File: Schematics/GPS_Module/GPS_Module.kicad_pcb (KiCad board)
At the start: 4 copper layers, 69.5 x 97.3 mm, 69 parts, among them J1 Stack Male Edge Connector, J2 SWD_01x04_Pin, J3 25SH-B-06-TR, J6 USB_B_Micro, Q1 AO3400A, SW1 SW_STM_RESET, SW2 SW_STM_BOOT_MODE, U1 STM32F103CBTx, U10 AMS1117-3.3, U3 W25Q128JVS, U4 LM66100DCKR, U5 LM66100DCKR, U6 LM66100DCKR, U7 ACS70331EOLC, U9 ISO1042BQDWVR, Y1 X322516MMB4SI

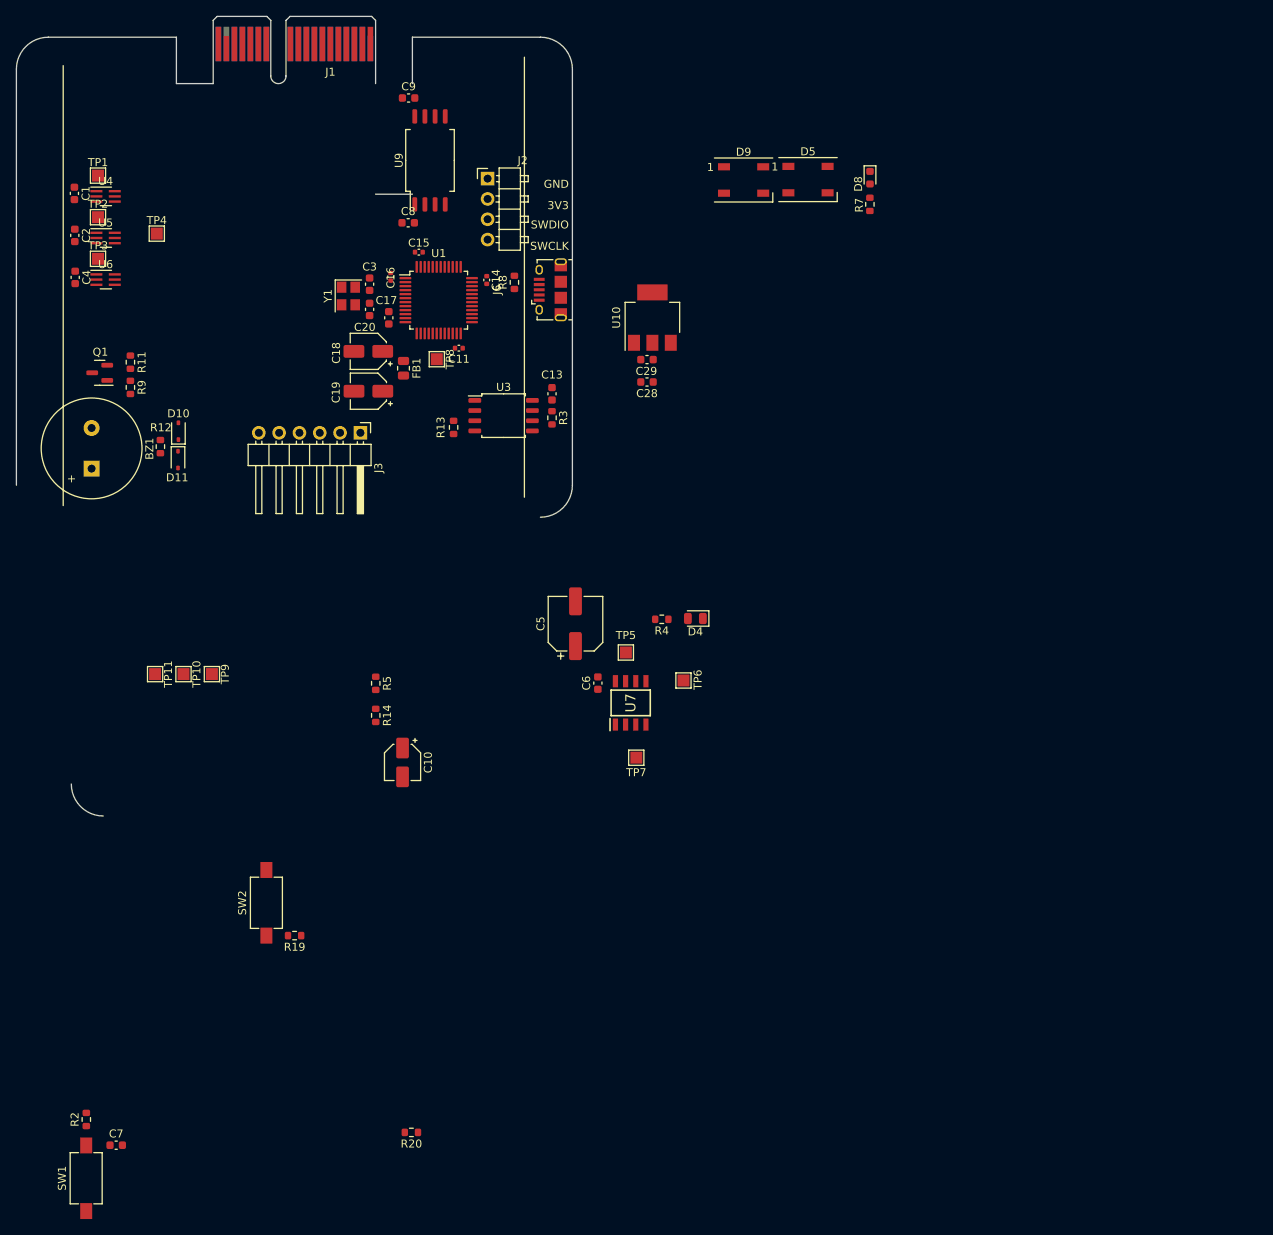
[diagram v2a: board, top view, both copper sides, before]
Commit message: Revert "starting PCB layout"
This reverts commit 0f9aa6cd92282e41b038e1a8acfc0611b64ad155.
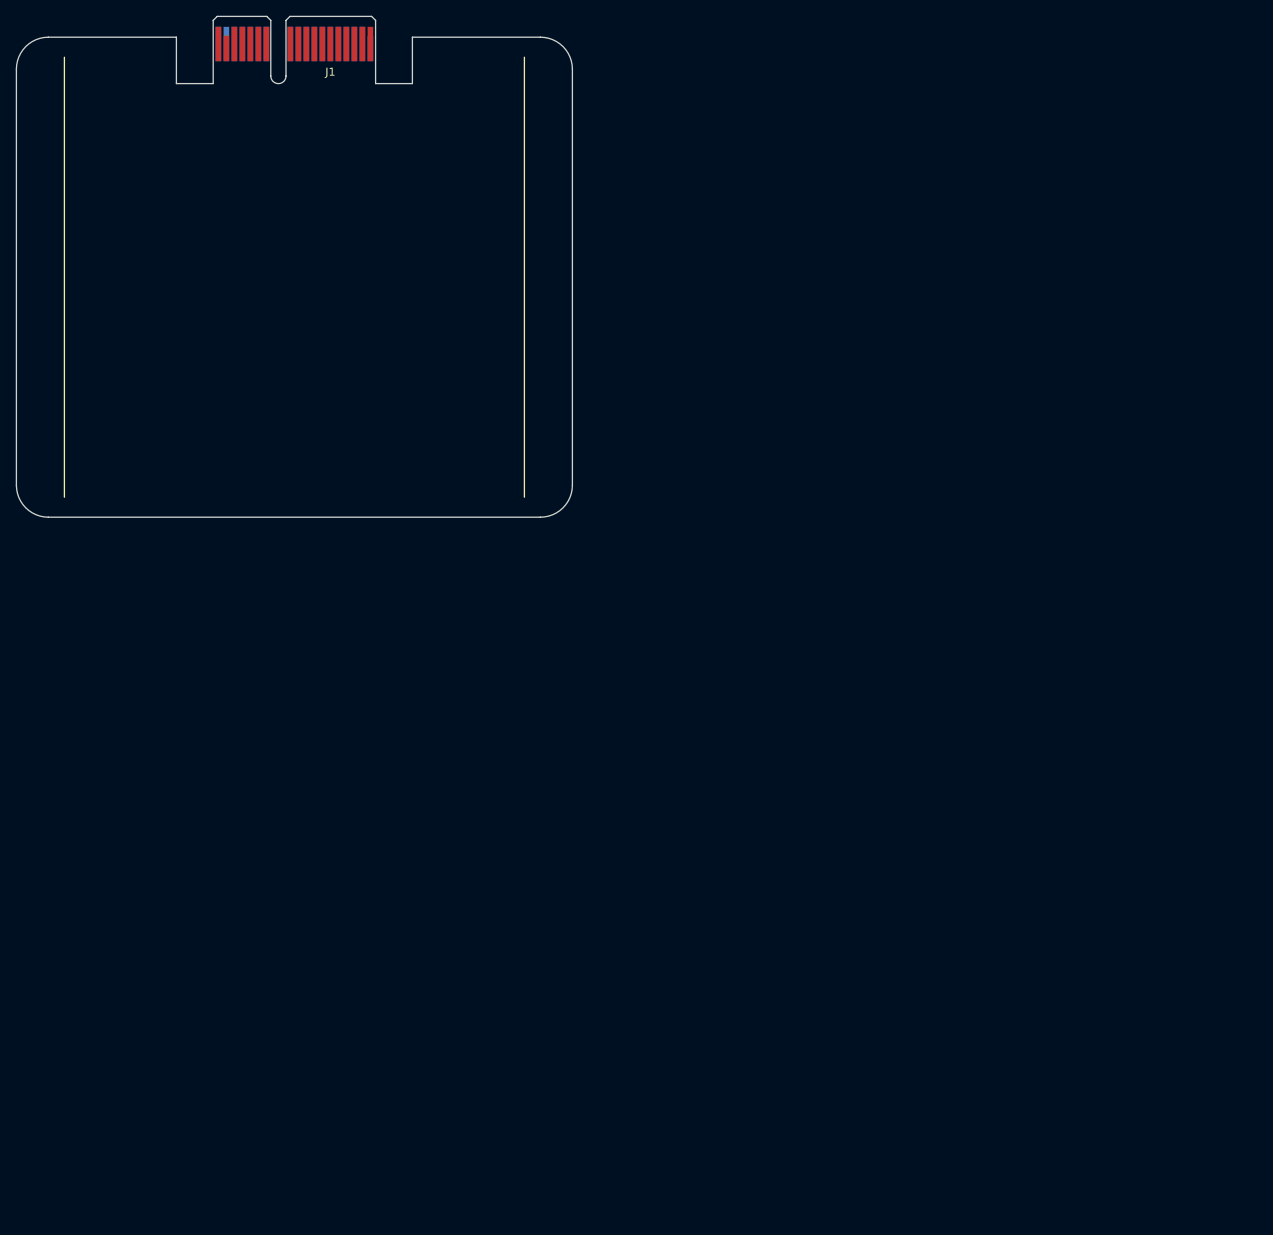
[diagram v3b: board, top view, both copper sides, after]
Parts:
- removed BZ1: PKM13EPYH4000, footprints:Buzzer_12.6x9.5RM5.0
- removed C1, C2, C4: 1uF, Capacitor_SMD:C_0603_1608Metric
- removed C10: 10u, Capacitor_SMD:CP_Elec_4x5.4
- removed C11, C14, C15, C16: 100n, Capacitor_SMD:C_0402_1005Metric
- removed C13, C7: 100nF, Capacitor_SMD:C_0603_1608Metric
- removed C17: 10n, Capacitor_SMD:C_0603_1608Metric
- removed C18, C19: 1uF, Capacitor_SMD:CP_Elec_4x5.4
- removed C20, C3: 10p, Capacitor_SMD:C_0603_1608Metric
- removed C28, C29: 10uF, Capacitor_SMD:C_0603_1608Metric
- removed C5: 100uF, Capacitor_SMD:CP_Elec_6.3x5.9
- removed C6: 0.1uF, Capacitor_SMD:C_0603_1608Metric
- removed C8, C9: 0.1u, Capacitor_SMD:C_0603_1608Metric
- removed D10, D11: 1N5819WS, Diode_SMD:D_SOD-323
- removed D4: PWR_LED (GRN), LED_SMD:LED_0805_2012Metric
- removed D5, D9: WS2812B, LED_SMD:LED_WS2812B_PLCC4_5.0x5.0mm_P3.2mm
- removed D8: DB_LED (YLW), LED_SMD:LED_0603_1608Metric
- removed FB1: 100R, Resistor_SMD:R_0805_2012Metric
- removed J2: SWD_01x04_Pin, SWD_Header:SWD_PinHeader_1x04_P2.54mm_Horizontal
- removed J3: 25SH-B-06-TR, Connector_PinHeader_2.54mm:PinHeader_1x06_P2.54mm_Horizontal
- removed J6: USB_B_Micro, Connector_USB:USB_Micro-B_Amphenol_10118194_Horizontal
- removed Q1: AO3400A, Package_TO_SOT_SMD:SOT-23
- removed R11, R13, R14, R2, R3: 10k, Resistor_SMD:R_0603_1608Metric
- removed R12: 1k, Resistor_SMD:R_0603_1608Metric
- removed R19, R20: 100k, Resistor_SMD:R_0603_1608Metric
- removed R4: 820R, Resistor_SMD:R_0603_1608Metric
- removed R5: 30k, Resistor_SMD:R_0603_1608Metric
- removed R7: 560R, Resistor_SMD:R_0603_1608Metric
- removed R8: 1.5k, Resistor_SMD:R_0603_1608Metric
- removed R9: 510R, Resistor_SMD:R_0603_1608Metric
- removed SW1: SW_STM_RESET, PTS636:PTS636_SK43_SMTR_LFS
- removed SW2: SW_STM_BOOT_MODE, PTS636:PTS636_SK43_SMTR_LFS
- removed TP1: TP_VSTACK, TestPoint:TestPoint_Pad_1.5x1.5mm
- removed TP10: TP_PA1, TestPoint:TestPoint_Pad_1.5x1.5mm
- removed TP11: TP_PA0, TestPoint:TestPoint_Pad_1.5x1.5mm
- removed TP2: TP_VUSB, TestPoint:TestPoint_Pad_1.5x1.5mm
- removed TP3: TP_VSWD, TestPoint:TestPoint_Pad_1.5x1.5mm
- removed TP4: TP_MUX, TestPoint:TestPoint_Pad_1.5x1.5mm
- removed TP5: TP_ISENSE, TestPoint:TestPoint_Pad_1.5x1.5mm
- removed TP6: TP_GND, TestPoint:TestPoint_Pad_1.5x1.5mm
- removed TP7: TP_3V3, TestPoint:TestPoint_Pad_1.5x1.5mm
- removed TP8: TP_BSENSE, TestPoint:TestPoint_Pad_1.5x1.5mm
- removed TP9: TP_PA2, TestPoint:TestPoint_Pad_1.5x1.5mm
- removed U1: STM32F103CBTx, Package_QFP:LQFP-48_7x7mm_P0.5mm
- removed U10: AMS1117-3.3, Package_TO_SOT_SMD:SOT-223-3_TabPin2
- removed U3: W25Q128JVS, Package_SO:SOIC-8_5.23x5.23mm_P1.27mm
- removed U4, U5, U6: LM66100DCKR, LMR66100:SC-70-6_Handsoldering
- removed U7: ACS70331EOLC, footprints:SOIC127P600X175-8N
- removed U9: ISO1042BQDWVR, ISO1042:SOIC-8 ISO1042BDWV
- removed Y1: X322516MMB4SI, Crystal:Crystal_SMD_3225-4Pin_3.2x2.5mm
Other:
- board size 69.5 x 97.3 mm -> 69.5 x 60 mm
- board text added: "GPS Daughterboard will be in a seperate project"

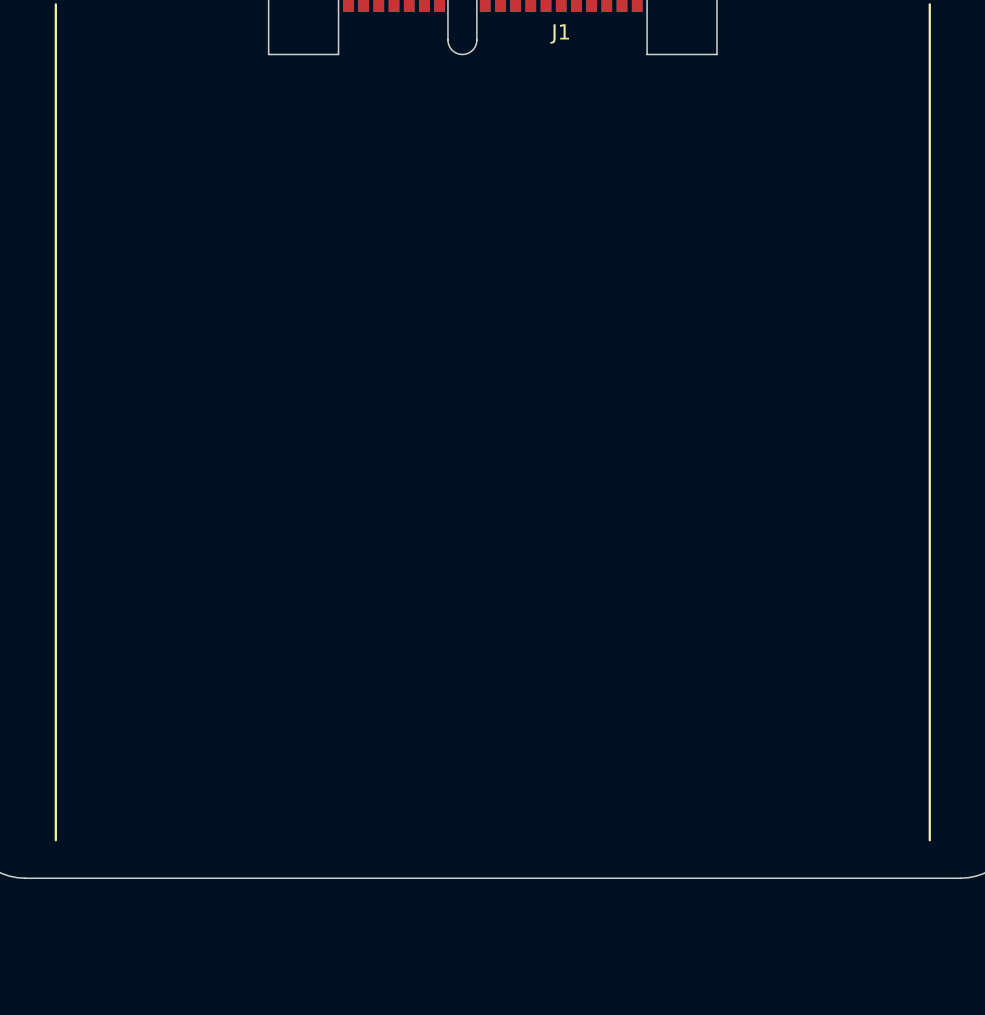
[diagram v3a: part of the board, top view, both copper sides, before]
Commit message: got everything on the board, starting wiring
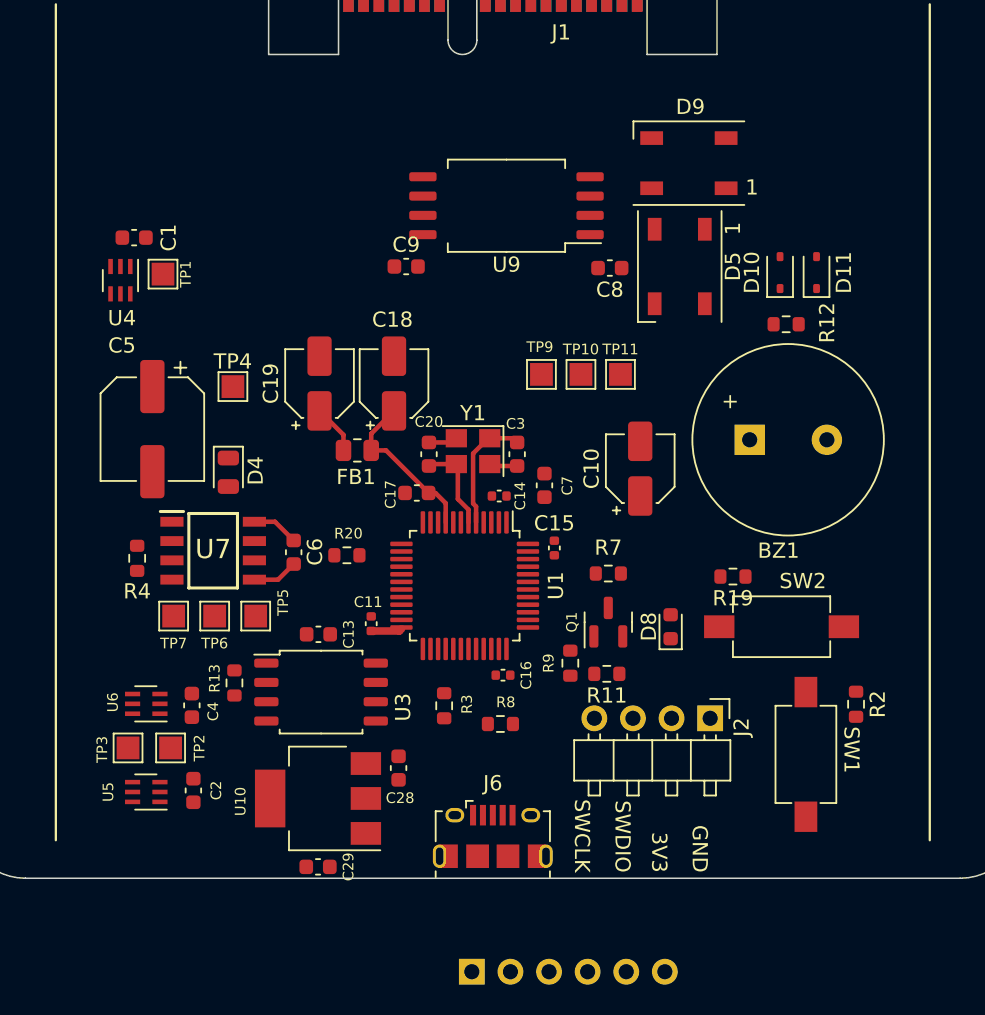
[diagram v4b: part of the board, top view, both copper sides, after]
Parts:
- added BZ1: PKM13EPYH4000, footprints:Buzzer_12.6x9.5RM5.0, F.Cu at (72.5, 51.3)
- added C1: 1uF, Capacitor_SMD:C_0603_1608Metric, F.Cu at (33.3, 38.0)
- added C10: 10u, Capacitor_SMD:CP_Elec_4x5.4, F.Cu at (66.6, 53.2)
- added C11: 100n, Capacitor_SMD:C_0402_1005Metric, F.Cu at (48.9, 63.4)
- added C13: 100nF, Capacitor_SMD:C_0603_1608Metric, F.Cu at (45.4, 64.1)
- added C14: 100n, Capacitor_SMD:C_0402_1005Metric, F.Cu at (57.3, 55.0)
- added C15: 100n, Capacitor_SMD:C_0402_1005Metric, F.Cu at (61.0, 58.4)
- added C16: 100n, Capacitor_SMD:C_0402_1005Metric, F.Cu at (57.6, 66.8)
- added C17: 10n, Capacitor_SMD:C_0603_1608Metric, F.Cu at (51.9, 54.8)
- added C18: 1uF, Capacitor_SMD:CP_Elec_4x5.4, F.Cu at (50.4, 47.6)
- added C19: 1uF, Capacitor_SMD:CP_Elec_4x5.4, F.Cu at (45.5, 47.6)
- added C2: 1uF, Capacitor_SMD:C_0603_1608Metric, F.Cu at (37.2, 74.4)
- added C20: 10p, Capacitor_SMD:C_0603_1608Metric, F.Cu at (52.7, 52.2)
- added C28: 10uF, Capacitor_SMD:C_0603_1608Metric, F.Cu at (50.7, 72.9)
- added C29: 10uF, Capacitor_SMD:C_0603_1608Metric, F.Cu at (45.4, 79.4)
- added C3: 10p, Capacitor_SMD:C_0603_1608Metric, F.Cu at (58.5, 52.2)
- added C4: 1uF, Capacitor_SMD:C_0603_1608Metric, F.Cu at (37.1, 68.8)
- added C5: 100uF, Capacitor_SMD:CP_Elec_6.3x5.9, F.Cu at (34.5, 50.6)
- added C6: 0.1uF, Capacitor_SMD:C_0603_1608Metric, F.Cu at (43.8, 58.7)
- added C7: 100nF, Capacitor_SMD:C_0603_1608Metric, F.Cu at (60.3, 54.3)
- added C8: 0.1u, Capacitor_SMD:C_0603_1608Metric, F.Cu at (64.6, 40.0)
- added C9: 0.1u, Capacitor_SMD:C_0603_1608Metric, F.Cu at (51.2, 39.9)
- added D10: 1N5819WS, Diode_SMD:D_SOD-323, F.Cu at (75.8, 40.3)
- added D11: 1N5819WS, Diode_SMD:D_SOD-323, F.Cu at (78.2, 40.3)
- added D4: PWR_LED (GRN), LED_SMD:LED_0805_2012Metric, F.Cu at (39.5, 53.4)
- added D5: WS2812B, LED_SMD:LED_WS2812B_PLCC4_5.0x5.0mm_P3.2mm, F.Cu at (69.2, 39.9)
- added D8: DB_LED (YLW), LED_SMD:LED_0603_1608Metric, F.Cu at (68.6, 63.6)
- added D9: WS2812B, LED_SMD:LED_WS2812B_PLCC4_5.0x5.0mm_P3.2mm, F.Cu at (69.8, 33.1)
- added FB1: 100R, Resistor_SMD:R_0805_2012Metric, F.Cu at (48.0, 52.0)
- added J2: SWD_01x04_Pin, SWD_Header:SWD_PinHeader_1x04_P2.54mm_Horizontal, F.Cu at (71.2, 69.6)
- added J3: 25SH-B-06-TR, Connector_PinHeader_2.54mm:PinHeader_1x06_P2.54mm_Horizontal, B.Cu at (55.5, 86.3)
- added J6: USB_B_Micro, Connector_USB:USB_Micro-B_Amphenol_10118194_Horizontal, F.Cu at (56.9, 77.4)
- added Q1: AO3400A, Package_TO_SOT_SMD:SOT-23, F.Cu at (64.5, 63.3)
- added R11: 10k, Resistor_SMD:R_0603_1608Metric, F.Cu at (64.4, 66.7)
- added R12: 1k, Resistor_SMD:R_0603_1608Metric, F.Cu at (76.2, 43.7)
- added R13: 10k, Resistor_SMD:R_0603_1608Metric, F.Cu at (39.9, 67.3)
- added R19: 100k, Resistor_SMD:R_0603_1608Metric, F.Cu at (72.7, 60.3)
- added R2: 10k, Resistor_SMD:R_0603_1608Metric, F.Cu at (80.8, 68.7)
- added R20: 100k, Resistor_SMD:R_0603_1608Metric, F.Cu at (47.3, 58.9)
- added R3: 10k, Resistor_SMD:R_0603_1608Metric, F.Cu at (53.7, 68.8)
- added R4: 820R, Resistor_SMD:R_0603_1608Metric, F.Cu at (33.5, 59.1)
- added R7: 560R, Resistor_SMD:R_0603_1608Metric, F.Cu at (64.5, 60.1)
- added R8: 1.5k, Resistor_SMD:R_0603_1608Metric, F.Cu at (57.4, 70.0)
- added R9: 510R, Resistor_SMD:R_0603_1608Metric, F.Cu at (62.0, 66.0)
- added SW1: SW_STM_RESET, PTS636:PTS636_SK43_SMTR_LFS, F.Cu at (77.5, 72.0)
- added SW2: SW_STM_BOOT_MODE, PTS636:PTS636_SK43_SMTR_LFS, F.Cu at (75.9, 63.6)
- added TP1: TP_VSTACK, TestPoint:TestPoint_Pad_1.5x1.5mm, F.Cu at (35.2, 40.4)
- added TP10: TP_PA1, TestPoint:TestPoint_Pad_1.5x1.5mm, F.Cu at (62.7, 47.0)
- added TP11: TP_PA0, TestPoint:TestPoint_Pad_1.5x1.5mm, F.Cu at (65.3, 47.0)
- added TP2: TP_VUSB, TestPoint:TestPoint_Pad_1.5x1.5mm, F.Cu at (35.7, 71.6)
- added TP3: TP_VSWD, TestPoint:TestPoint_Pad_1.5x1.5mm, F.Cu at (32.9, 71.6)
- added TP4: TP_MUX, TestPoint:TestPoint_Pad_1.5x1.5mm, F.Cu at (39.8, 47.8)
- added TP5: TP_ISENSE, TestPoint:TestPoint_Pad_1.5x1.5mm, F.Cu at (41.3, 62.9)
- added TP6: TP_GND, TestPoint:TestPoint_Pad_1.5x1.5mm, F.Cu at (38.6, 62.9)
- added TP7: TP_3V3, TestPoint:TestPoint_Pad_1.5x1.5mm, F.Cu at (35.9, 62.9)
- added TP9: TP_PA2, TestPoint:TestPoint_Pad_1.5x1.5mm, F.Cu at (60.1, 47.0)
- added U1: STM32F103CBTx, Package_QFP:LQFP-48_7x7mm_P0.5mm, F.Cu at (55.0, 60.9)
- added U10: AMS1117-3.3, Package_TO_SOT_SMD:SOT-223-3_TabPin2, F.Cu at (45.4, 74.9)
- added U3: W25Q128JVS, Package_SO:SOIC-8_5.23x5.23mm_P1.27mm, F.Cu at (45.6, 67.9)
- added U4: LM66100DCKR, LMR66100:SC-70-6, F.Cu at (32.4, 40.8)
- added U5: LM66100DCKR, LMR66100:SC-70-6, F.Cu at (34.1, 74.5)
- added U6: LM66100DCKR, LMR66100:SC-70-6, F.Cu at (34.1, 68.7)
- added U7: ACS70331EOLC, footprints:SOIC127P600X175-8N, F.Cu at (38.5, 58.6)
- added U9: ISO1042BQDWVR, ISO1042:SOIC-8 ISO1042BDWV, F.Cu at (57.8, 35.9)
- added Y1: X322516MMB4SI, Crystal:Crystal_SMD_3225-4Pin_3.2x2.5mm, F.Cu at (55.6, 52.0)
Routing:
- net +3.3VA: track 0.00 -> 10.8 mm
- net OSC_IN: track 0.00 -> 8.04 mm
- net GND: track 0.00 -> 6.92 mm
- net OSC_OUT: track 0.00 -> 6.02 mm
- net +3.3V: track 0.00 -> 5.09 mm
- net V_MUX: track 0.00 -> 3.10 mm

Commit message: finished PCB routing, waitting for approval
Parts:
- moved R11 21.7 mm to (62.5, 45.1), turned to 0 degrees
- moved Q1 15.5 mm to (62.5, 47.9), turned to -90 degrees
- moved R9 15.4 mm to (62.6, 50.6), turned to 180 degrees
- moved TP10 14.3 mm to (49.5, 41.6)
- moved TP11 14.3 mm to (52.1, 41.6)
- moved TP9 14.2 mm to (47.0, 41.6)
- moved TP4 11.0 mm to (32.0, 55.6)
- moved R19 5.77 mm to (71.8, 66.0), turned to 90 degrees
- moved R4 5.41 mm to (36.0, 54.3), turned to 180 degrees
- moved R7 5.00 mm to (68.5, 63.1)
- moved J3 4.83 mm to (51.8, 83.2)
- moved BZ1 4.43 mm to (68.4, 49.7)
- moved C8 4.00 mm to (60.6, 39.9), turned to 0 degrees
- moved C9 4.00 mm to (55.2, 39.9), turned to 180 degrees
- moved C13 3.99 mm to (42.1, 66.3), turned to 90 degrees
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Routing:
- net +3.3V: track 5.09 -> 215.5 mm, vias 0 -> 16
- net GND: track 6.92 -> 148.5 mm, vias 0 -> 30
- net DB_LED: track 0.00 -> 96.8 mm, vias 0 -> 1
- net V_MUX: track 3.10 -> 56.4 mm
- net V_PSU: track 0.00 -> 47.4 mm, vias 0 -> 3
- net V_SWD: track 0.00 -> 38.1 mm, vias 0 -> 2
- net STM_RESET: track 0.00 -> 36.1 mm, vias 0 -> 2
- net CAN_RX: track 0.00 -> 35.7 mm
- net RGB_DATA: track 0.00 -> 34.9 mm
- net CAN_TX: track 0.00 -> 33.4 mm
- net +5V: track 0.00 -> 33.0 mm, vias 0 -> 1
- net Net-(U1-PA1): track 0.00 -> 28.6 mm
- net V_BATT: track 0.00 -> 26.6 mm
- net SDA_GPS: track 0.00 -> 25.9 mm, vias 0 -> 1
- net RST_GPS: track 0.00 -> 24.6 mm, vias 0 -> 1
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- added copper zone on F.Cu, net +3.3V
- added copper zone on F.Cu, net /USB_5V
- added copper zone on F.Cu, net GND
- added copper zone on F.Cu, net V_MUX
- added copper zone on F.Cu, net V_REGUSB
